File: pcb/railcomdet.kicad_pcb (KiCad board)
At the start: 4 copper layers, 110 x 70 mm, 162 parts, among them J1 MVE252-5-V, J10 MVE252-5-V, J2 MVE252-5-V, J3 MVE252-5-V, J4 MVE252-5-V, J5 MVE252-5-V, J6 PINHEADER, J7 PINHEADER, J8 PROG/DEBUG, J9 MVE252-5-V, SW1 6x6, U1 VO0631T, U10 LM339, U11 LM339, U12 STM32F103C8Tx, U13 AMS1117-3.3, U14 L78L05_SOT89, U15 SN75176AP, U2 VO0631T, U3 VO0631T, U4 L78L05_SOT89, U5 L79L05_SOT89, U6 LM339, U7 LM339, U8 LM339, U9 4052, Y1 14,7456MHz

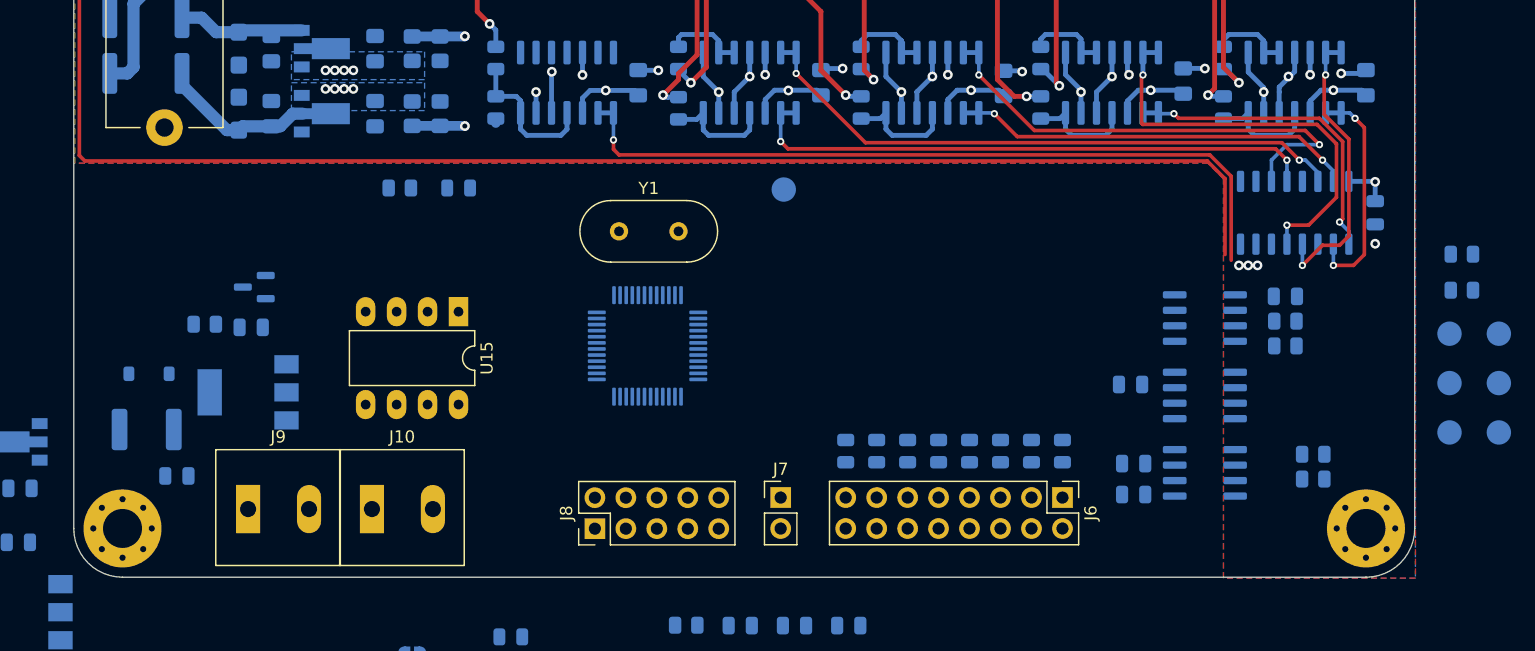
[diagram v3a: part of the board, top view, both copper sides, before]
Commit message: Add filled zone to MTB part.
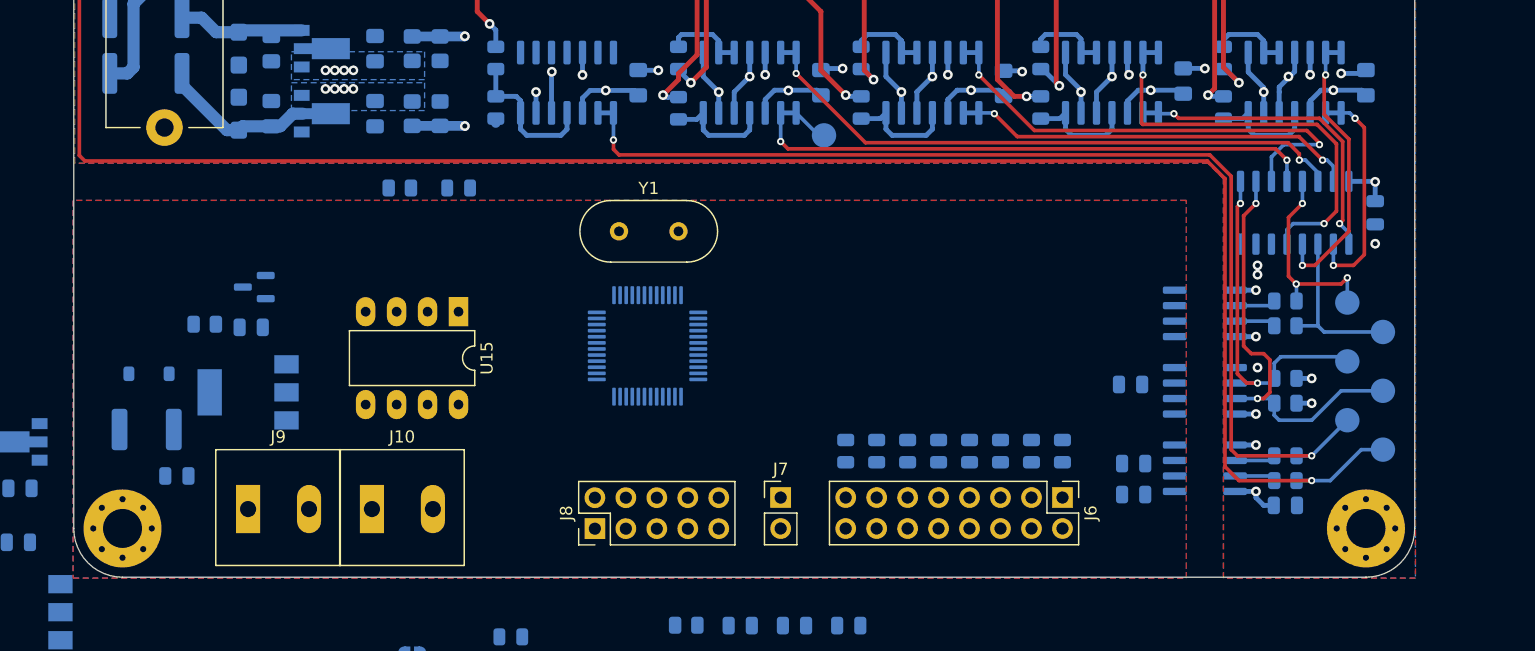
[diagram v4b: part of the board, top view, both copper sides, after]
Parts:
- moved C1 17.1 mm to (199.4, 94.1)
- moved R4 15.0 mm to (199.4, 77.3)
- moved R5 14.8 mm to (199.4, 79.4)
- moved TP1 12.7 mm to (204.5, 77.5)
- moved U3 12.3 mm to (192.8, 91.1)
- moved R2 11.0 mm to (199.4, 90.0)
- moved R3 11.0 mm to (199.4, 92.1)
- moved TP2 10.4 mm to (207.4, 79.9)
- moved TP3 10.1 mm to (207.4, 84.7)
- moved TP5 8.92 mm to (204.5, 87.1)
- moved TP4 8.68 mm to (204.5, 82.3)
- moved R1 8.57 mm to (199.4, 83.7)
- moved U2 6.73 mm to (192.8, 78.4)
- moved U1 6.73 mm to (192.8, 84.7)
- moved TP6 5.64 mm to (207.4, 89.5)
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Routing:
- net /DCC/MULT1: track 0.00 -> 34.9 mm, vias 0 -> 2
- net KOUT: track 128.8 -> 162.0 mm, vias 1 -> 2
- net /DCC/MULT2: track 0.00 -> 28.8 mm, vias 0 -> 2
- net /DCC/CUTOUT: track 62.7 -> 90.5 mm, vias 1 -> 2
- net /DCC/TX1: track 0.00 -> 17.0 mm, vias 0 -> 3
- net /DCC/TX2: track 0.00 -> 14.0 mm
- net +5VA: track 34.3 -> 47.6 mm, vias 10 -> 17
- net Net-(U3-C2): track 0.00 -> 3.37 mm
- net Net-(U3-C1): track 0.00 -> 3.37 mm
- net Net-(U2-C2): track 0.00 -> 3.37 mm
- net Net-(U2-C1): track 0.00 -> 3.37 mm
- net Net-(U9-X0): track 47.5 -> 50.6 mm
- added copper zone on In1.Cu, net +3V3
- added copper zone on B.Cu, net GND
- added copper zone on F.Cu, net GND
- added copper zone on In2.Cu, net GND

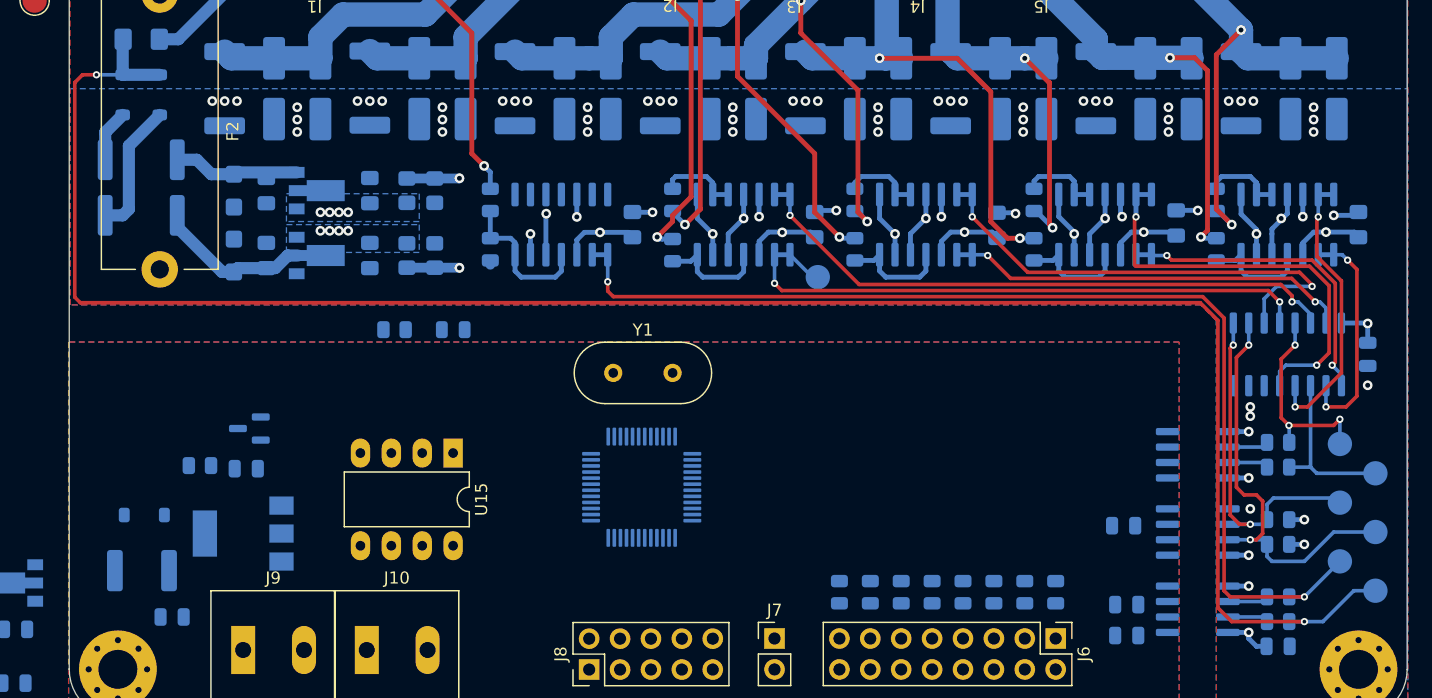
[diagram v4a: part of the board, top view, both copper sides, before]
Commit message: pcb: use THT testpins for DCC part.
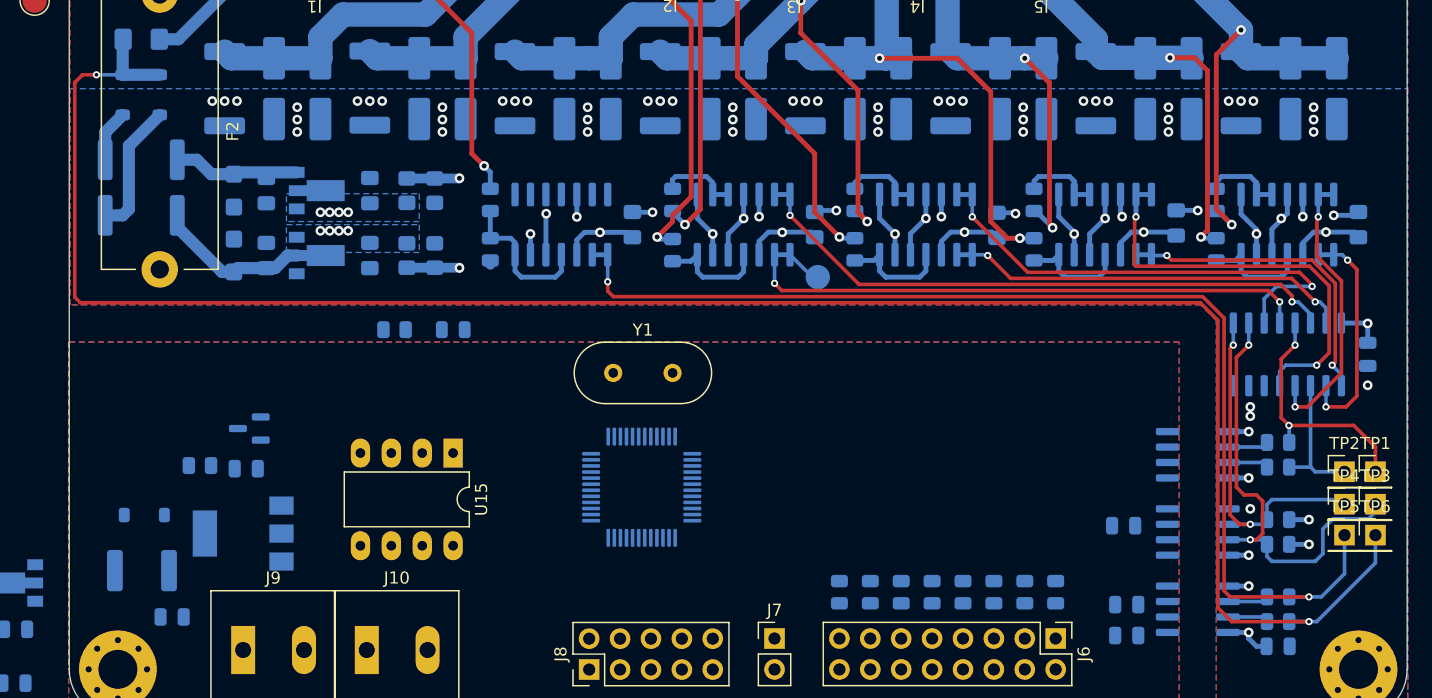
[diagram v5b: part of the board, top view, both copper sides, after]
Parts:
- TP1, TP2, TP3, TP4, TP5, TP6: footprint TestPoint:TestPoint_Pad_D2.0mm -> Connector_PinHeader_2.54mm:PinHeader_1x01_P2.54mm_Vertical; moved to F.Cu
- moved TP6 4.57 mm to (207.4, 85.0), turned to 0 degrees
- moved TP1 3.71 mm to (207.4, 79.8), turned to 0 degrees
- moved TP2 2.54 mm to (204.9, 79.8), turned to 0 degrees
- moved TP3 2.29 mm to (207.4, 82.4), turned to 0 degrees
- moved TP5 2.19 mm to (204.9, 85.0), turned to 0 degrees
- moved TP4 0.40 mm to (204.9, 82.4), turned to 0 degrees
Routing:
- net KOUT: track 162.0 -> 165.6 mm
- net /DCC/CUTOUT: track 90.5 -> 94.0 mm
- net /DCC/TX1: track 17.0 -> 20.4 mm, vias 3 -> 2
- net /DCC/TX2: track 14.0 -> 11.4 mm
- net /DCC/MULT1: track 34.9 -> 37.4 mm
- net +5VA: track 47.6 -> 48.3 mm

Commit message: pcb: everything routed.
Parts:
- C24, C25, C26: footprint Capacitor_SMD:C_0805_2012Metric -> Capacitor_SMD:C_0805_2012Metric_Pad1.18x1.45mm_HandSolder
- D3, D4, D5, D6: moved to F.Cu
- JP1, JP2: footprint Jumper:SolderJumper-2_P1.3mm_Open_RoundedPad1.0x1.5mm -> Connector_PinHeader_2.54mm:PinHeader_1x02_P2.54mm_Vertical
- TP10, TP11, TP12, TP7, TP8, TP9: footprint TestPoint:TestPoint_Pad_D2.0mm -> Connector_PinHeader_2.54mm:PinHeader_1x01_P2.54mm_Vertical
- TP16, TP17, TP18: footprint TestPoint:TestPoint_Pad_D2.0mm -> Connector_PinHeader_2.54mm:PinHeader_1x01_P2.54mm_Vertical; moved to F.Cu
- moved TP12 105.7 mm to (186.3, 97.4)
- moved R12 104.8 mm to (185.9, 90.0)
- moved TP10 104.8 mm to (186.3, 80.6)
- moved TP11 103.9 mm to (183.8, 97.4)
- moved R11 102.5 mm to (185.9, 78.1), turned to 0 degrees
- moved R13 100.9 mm to (182.1, 92.3), turned to 0 degrees
- moved TP14 100.5 mm to (196.6, 35.6)
- moved TP7 100.2 mm to (186.3, 71.9)
- moved R10 98.7 mm to (185.9, 92.3), turned to 0 degrees
- moved R8 98.5 mm to (185.9, 85.5), turned to 0 degrees
- moved TP8 97.8 mm to (183.8, 71.9)
- moved TP9 97.6 mm to (183.8, 80.6)
- moved R9 97.4 mm to (185.9, 83.2), turned to 0 degrees
- moved R7 97.1 mm to (185.9, 75.8), turned to 0 degrees
- moved TP15 52.5 mm to (130.7, 72.4)
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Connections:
- SW1 pad 2: GND -> Net-(U12-PB15)
- U12 pad 28: Net-(SW1-A) -> Net-(U12-PB15)
- U15 pad 3: MTB-TX -> MTB-TE
- U15 pad 4: MTB-TE -> MTB-TX
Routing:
- net +5V: track 0.00 -> 122.4 mm, vias 0 -> 17
- net MTB-TX: track 0.00 -> 59.1 mm, vias 0 -> 1
- net MTB-RX: track 0.00 -> 55.2 mm, vias 0 -> 1
- net +3V3: track 0.00 -> 52.3 mm, vias 0 -> 29
- net MTB-TE: track 0.00 -> 47.6 mm, vias 0 -> 2
- net /MTB/RX1: track 0.00 -> 38.6 mm, vias 0 -> 2
- net ADDR-128: track 0.00 -> 37.3 mm, vias 0 -> 1
- net /MTB/DCC: track 0.00 -> 35.3 mm, vias 0 -> 2
- net ADDR-64: track 0.00 -> 34.5 mm, vias 0 -> 1
- net /MTB/RX2: track 0.00 -> 33.2 mm, vias 0 -> 2
- net ADDR-4: track 0.00 -> 33.0 mm, vias 0 -> 1
- net Net-(D7-A): track 0.00 -> 32.9 mm
- net ADDR-1: track 0.00 -> 32.8 mm, vias 0 -> 1
- net ADDR-2: track 0.00 -> 32.5 mm, vias 0 -> 1
- net ADDR-32: track 0.00 -> 32.0 mm, vias 0 -> 1
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- added copper zone on B.Cu, net +3V3
- added copper zone on B.Cu, net +5V
- added copper zone on In1.Cu, net +5V

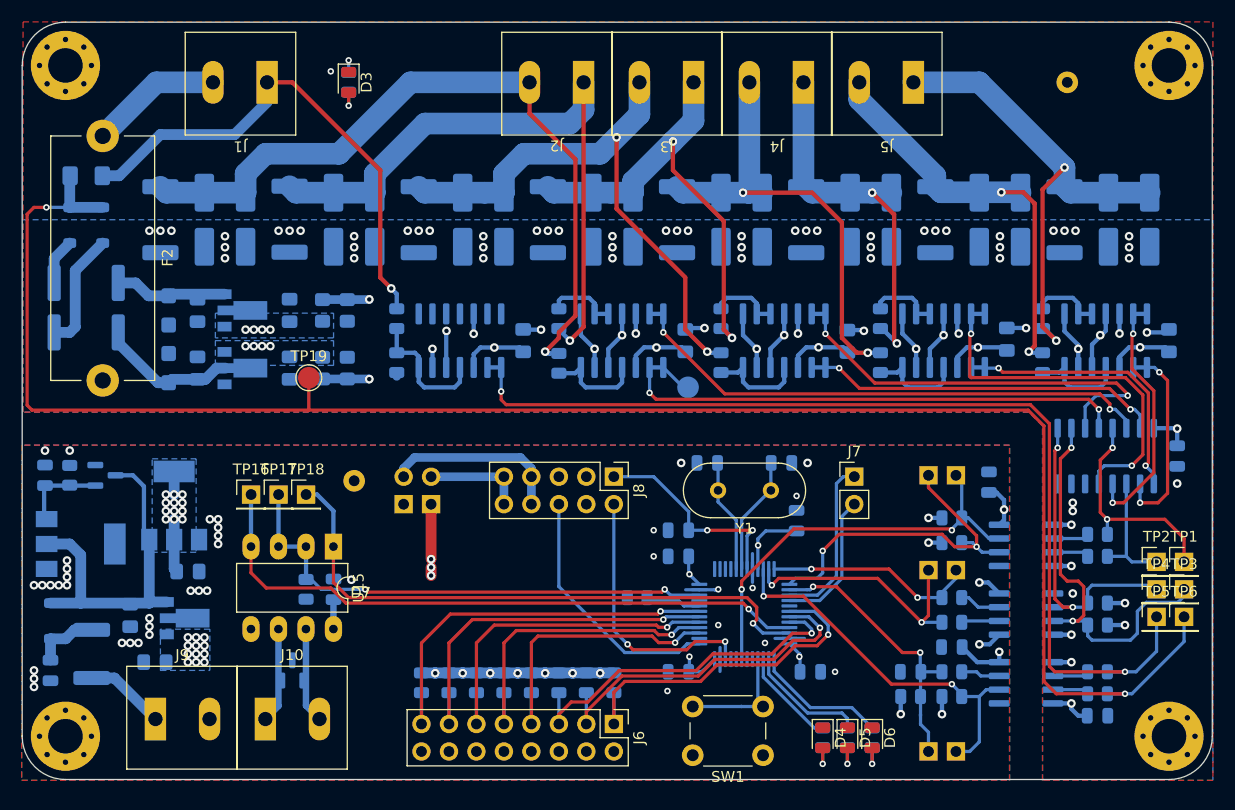
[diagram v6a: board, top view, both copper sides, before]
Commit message: Use handsolder SMDs where possible.
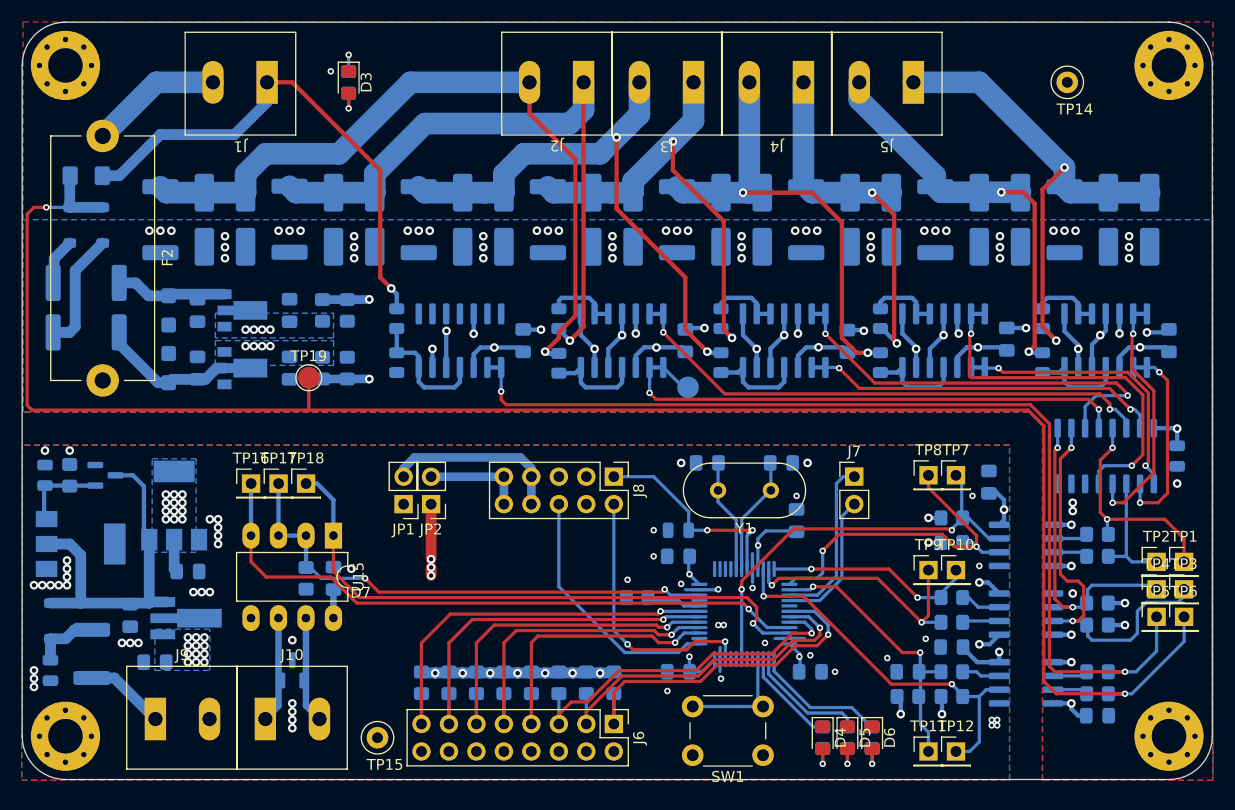
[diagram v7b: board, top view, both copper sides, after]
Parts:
- C1, C17, C18, C19, C2, C20, C22, C23, C27, C3, C4: footprint Capacitor_SMD:C_0805_2012Metric -> Capacitor_SMD:C_0805_2012Metric_Pad1.18x1.45mm_HandSolder
- D3, D4, D5, D6: footprint LED_SMD:LED_0805_2012Metric -> LED_SMD:LED_0805_2012Metric_Pad1.15x1.40mm_HandSolder
- JP1, JP2, TP10, TP11, TP12, TP14, TP15, TP7, TP8, TP9: moved to F.Cu
- R1, R10, R11, R12, R13, R2, R28, R3, R39, R4, R40, R41, R42, R43, R44, R45, R46, R47, R48, R49, R5, R50, R51, R52, R6, R7, R8, R9: footprint Resistor_SMD:R_0805_2012Metric -> Resistor_SMD:R_0805_2012Metric_Pad1.20x1.40mm_HandSolder
- R18, R19: footprint Resistor_SMD:R_2512_6332Metric -> Resistor_SMD:R_2512_6332Metric_Pad1.40x3.35mm_HandSolder
- U14: footprint Package_TO_SOT_SMD:SOT-89-3 -> Package_TO_SOT_SMD:SOT-89-3_Handsoldering
- moved TP15 23.8 mm to (132.8, 96.1), turned to 0 degrees
- moved C27 1.02 mm to (128.8, 81.4)
- moved R43 1.02 mm to (126.2, 81.4)
- moved U15 1.02 mm to (128.8, 77.5)
- moved TP16 1.02 mm to (121.2, 72.6)
- moved TP17 1.02 mm to (123.7, 72.6)
- moved TP18 1.02 mm to (126.2, 72.6)
- moved C4 0.25 mm to (181.9, 90.0)
- moved R13 0.25 mm to (181.9, 92.3)
- moved U14 0.13 mm to (115.4, 85.1)
- turned JP1 to 180 degrees
- turned JP2 to 180 degrees
- turned TP10 to 0 degrees
- turned TP11 to 0 degrees
- turned TP12 to 0 degrees
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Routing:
- net +3V3: track 52.3 -> 48.2 mm
- net +5V: track 122.4 -> 121.8 mm
- net Net-(D3-A): track 2.47 -> 2.98 mm
- net +5VA: track 49.5 -> 50.0 mm
- net GND: vias 39 -> 54

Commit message: pcb: silkscreen top.
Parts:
- moved C17 1.44 mm to (170.6, 77.1), turned to 0 degrees
- moved R40 1.08 mm to (157.6, 82.4), turned to 90 degrees
- moved TP16 0.65 mm to (121.2, 72.0)
- moved TP17 0.65 mm to (123.7, 72.0)
- moved TP18 0.65 mm to (126.2, 72.0)
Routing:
- net +3V3: track 48.2 -> 45.8 mm
- net /MTB/DCC: track 35.3 -> 33.9 mm
- net SWCLK: track 23.5 -> 24.5 mm
- net MTB-TE: track 48.0 -> 49.0 mm
- net MTB-TX: track 59.5 -> 60.4 mm
- net MTB-RX: track 55.6 -> 56.2 mm
- net GNDA: vias 53 -> 55
- net GND: vias 54 -> 60
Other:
- board text added: "1"
- board text added: "128"
- board text added: "12V"
- board text added: "16"
- board text added: "2"
- board text added: "32"
- board text added: "3V3"
- board text added: "4"
- board text added: "5V"
- board text added: "64"
- board text added: "8"
- board text added: "A"
- board text added: "B"
- board text added: "CUT"
- board text added: "CUTOUT"
- board text added: "DCC"
- board text added: "GND"
- board text added: "GNDA"
- board text added: "J"
- board text added: "J1"
- board text added: "J2"
- board text added: "J3"
- board text added: "J4"
- board text added: "J5"
- board text added: "J6"
- board text added: "J7"
- board text added: "J8"
- board text added: "K"
- board text added: "KOU"
- board text added: "MTB addr"
- board text added: "MU1"
- board text added: "MU2"
- board text added: "MULT1"
- board text added: "MULT2"
- board text added: "NC"
- board text added: "RST"
- board text added: "RX"
- board text added: "RX1"
- board text added: "RX2"
- board text added: "STLINK"
- board text added: "SWCLK"
- board text added: "SWDIO"
- board text added: "TE"
- board text added: "TX"
- board text added: "TX1"
- board text added: "TX2"
